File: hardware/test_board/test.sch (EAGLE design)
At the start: 25 parts, among them IC2 MAX707CPA, IC3 74HCT573N, IC5 7805DT, J2 POWER_JACKSLT

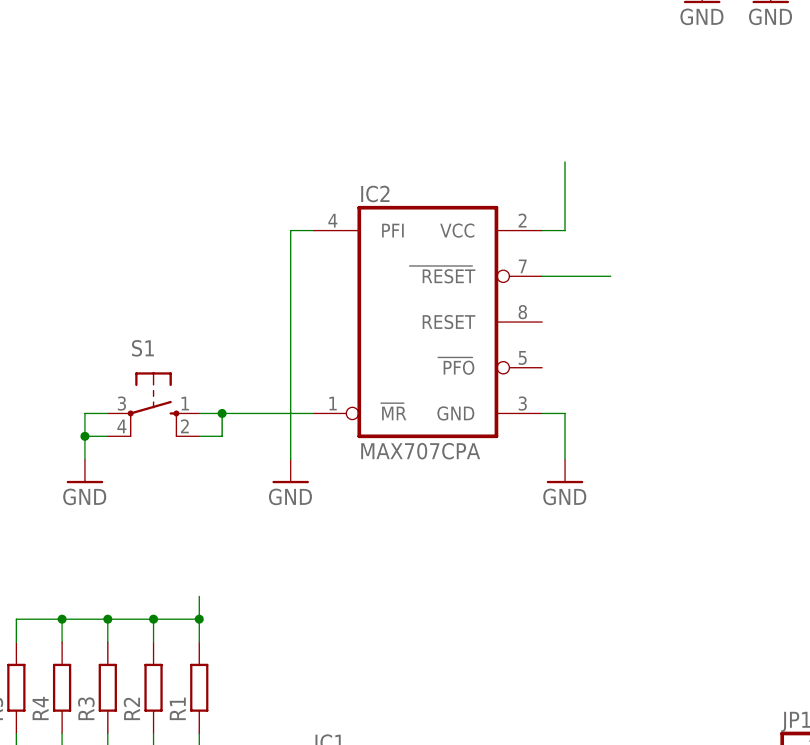
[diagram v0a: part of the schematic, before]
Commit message: RST circuit simplified according to datasheet
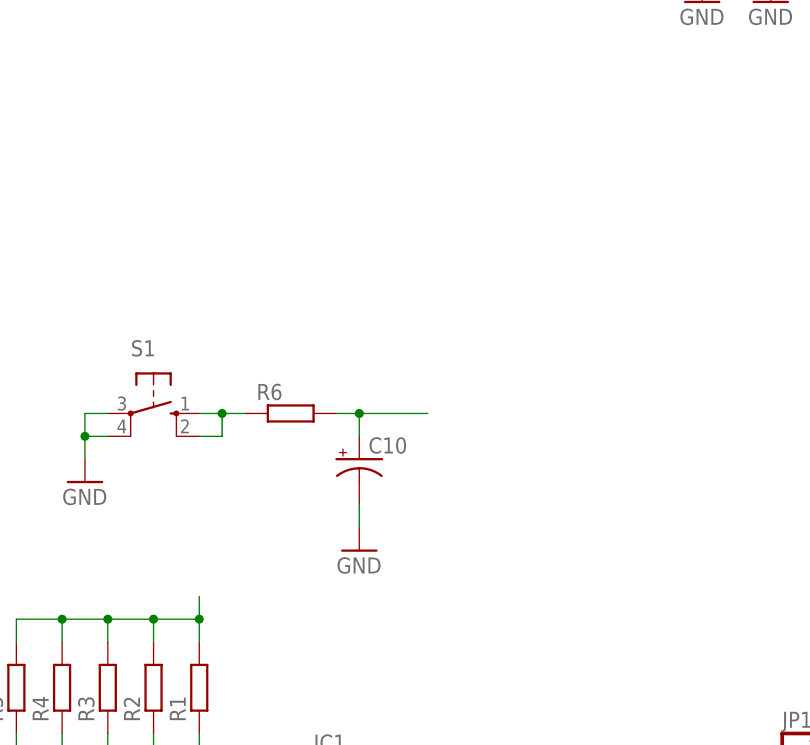
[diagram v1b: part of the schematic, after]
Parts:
- removed IC2: MAX707CPA, maxim:MAX707CPA
- added C10: (no value), rcl:CPOL-USE2,5-6E
- added R6: (no value), rcl:R-EU_R0603
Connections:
- net !RESET: now also C10.+, R6.2; no longer IC2.RESET
- net GND: now also C10.-; no longer IC2.GND, IC2.PFI
- net N$8: now also R6.1; no longer IC2.MR
- net VCC: no longer IC2.VCC
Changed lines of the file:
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@@
 <part name="C3" library="rcl" deviceset="C-EU" device="C0603"/>
 <part name="C4" library="rcl" deviceset="C-EU" device="C0603"/>
-<part name="IC2" library="maxim" deviceset="MAX707CPA" device=""/>
 <part name="GND7" library="supply1" deviceset="GND" device=""/>
-<part name="GND8" library="supply1" deviceset="GND" device=""/>
 <part name="S1" library="switch-omron" deviceset="10-XX" device=""/>
 <part name="GND9" library="supply1" deviceset="GND" device=""/>
@@
 <part name="C9" library="rcl" deviceset="C-EU" device="C0603"/>
 <part name="GND15" library="supply1" deviceset="GND" device=""/>
+<part name="R6" library="rcl" deviceset="R-EU_" device="R0603"/>
+<part name="C10" library="rcl" deviceset="CPOL-US" device="E2,5-6E"/>
 </parts>
 <sheets>
@@
 <instance part="C3" gate="G$1" x="152.4" y="27.94"/>
 <instance part="C4" gate="G$1" x="160.02" y="27.94"/>
-<instance part="IC2" gate="G$1" x="20.32" y="142.24"/>
-<instance part="GND7" gate="1" x="5.08" y="124.46"/>
-<instance part="GND8" gate="1" x="35.56" y="124.46"/>
+<instance part="GND7" gate="1" x="12.7" y="116.84"/>
 <instance part="S1" gate="1" x="-10.16" y="132.08" rot="R270"/>
 <instance part="GND9" gate="1" x="-17.78" y="124.46"/>
@@
 <instance part="C9" gate="G$1" x="167.64" y="27.94"/>
 <instance part="GND15" gate="1" x="55.88" y="63.5"/>
+<instance part="R6" gate="G$1" x="5.08" y="132.08"/>
+<instance part="C10" gate="G$1" x="12.7" y="127"/>
 </instances>
 <busses>
@@
 </segment>
 <segment>
-<pinref part="IC2" gate="G$1" pin="PFI"/>
-<pinref part="GND7" gate="1" pin="GND"/>
-<wire x1="7.62" y1="152.4" x2="5.08" y2="152.4" width="0.1524" layer="91"/>
-<wire x1="5.08" y1="152.4" x2="5.08" y2="127" width="0.1524" layer="91"/>
-</segment>
-<segment>
-<pinref part="IC2" gate="G$1" pin="GND"/>
-<pinref part="GND8" gate="1" pin="GND"/>
-<wire x1="33.02" y1="132.08" x2="35.56" y2="132.08" width="0.1524" layer="91"/>
-<wire x1="35.56" y1="132.08" x2="35.56" y2="127" width="0.1524" layer="91"/>
-</segment>
-<segment>
 <pinref part="S1" gate="1" pin="P"/>
 <pinref part="GND9" gate="1" pin="GND"/>
@@
 <wire x1="63.5" y1="93.98" x2="55.88" y2="93.98" width="0.1524" layer="91"/>
 <wire x1="55.88" y1="93.98" x2="55.88" y2="66.04" width="0.1524" layer="91"/>
+</segment>
+<segment>
+<pinref part="GND7" gate="1" pin="GND"/>
+<pinref part="C10" gate="G$1" pin="-"/>
+<wire x1="12.7" y1="119.38" x2="12.7" y2="121.92" width="0.1524" layer="91"/>
 </segment>
 </net>
@@
 </segment>
 <segment>
-<pinref part="IC2" gate="G$1" pin="VCC"/>
-<wire x1="33.02" y1="152.4" x2="35.56" y2="152.4" width="0.1524" layer="91"/>
-<wire x1="35.56" y1="152.4" x2="35.56" y2="160.02" width="0.1524" layer="91"/>
-</segment>
-<segment>
 <pinref part="IC5" gate="A1" pin="VO"/>
 <wire x1="86.36" y1="193.04" x2="88.9" y2="193.04" width="0.1524" layer="91"/>
@@
 <net name="!RESET" class="0">
 <segment>
-<pinref part="IC2" gate="G$1" pin="RESET"/>
-<wire x1="33.02" y1="147.32" x2="40.64" y2="147.32" width="0.1524" layer="91"/>
-</segment>
-<segment>
 <pinref part="IC1" gate="G$1" pin="RESET"/>
 <wire x1="2.54" y1="83.82" x2="0" y2="83.82" width="0.1524" layer="91"/>
 </segment>
-</net>
-<net name="N$8" class="0">
-<segment>
-<pinref part="IC2" gate="G$1" pin="MR"/>
-<wire x1="7.62" y1="132.08" x2="-2.54" y2="132.08" width="0.1524" layer="91"/>
-<pinref part="S1" gate="1" pin="S"/>
-<pinref part="S1" gate="1" pin="S1"/>
-<wire x1="-2.54" y1="132.08" x2="-5.08" y2="132.08" width="0.1524" layer="91"/>
-<wire x1="-5.08" y1="129.54" x2="-2.54" y2="129.54" width="0.1524" layer="91"/>
-<wire x1="-2.54" y1="129.54" x2="-2.54" y2="132.08" width="0.1524" layer="91"/>
-<junction x="-2.54" y="132.08"/>
+<segment>
+<pinref part="R6" gate="G$1" pin="2"/>
+<pinref part="C10" gate="G$1" pin="+"/>
+<wire x1="10.16" y1="132.08" x2="12.7" y2="132.08" width="0.1524" layer="91"/>
+<wire x1="12.7" y1="132.08" x2="12.7" y2="129.54" width="0.1524" layer="91"/>
+<wire x1="12.7" y1="132.08" x2="20.32" y2="132.08" width="0.1524" layer="91"/>
+<junction x="12.7" y="132.08"/>
 </segment>
 </net>
@@
 </segment>
 </net>
+<net name="N$8" class="0">
+<segment>
+<pinref part="S1" gate="1" pin="S"/>
+<wire x1="-5.08" y1="132.08" x2="-2.54" y2="132.08" width="0.1524" layer="91"/>
+<pinref part="S1" gate="1" pin="S1"/>
+<wire x1="-5.08" y1="129.54" x2="-2.54" y2="129.54" width="0.1524" layer="91"/>
+<wire x1="-2.54" y1="129.54" x2="-2.54" y2="132.08" width="0.1524" layer="91"/>
+<pinref part="R6" gate="G$1" pin="1"/>
+<wire x1="0" y1="132.08" x2="-2.54" y2="132.08" width="0.1524" layer="91"/>
+<junction x="-2.54" y="132.08"/>
+</segment>
+</net>

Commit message: Minor optimizations
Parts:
- removed IC4: (no value), memory:2716
- removed JP1: (no value), pinhead:PINHD-1X10
- added C11: (no value), rcl:C-EUC0603
- added IC2: (no value), memory:2732
- added JP2: (no value), pinhead:PINHD-1X15
- R1, R2, R3, R5: device rcl:R-EU_R0603 -> rcl:R-EU_R1206
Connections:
- removed net N$7: IC1.INT, R5.1
- new net A11: IC1.P23, IC2A.A11
- new net INT: IC1.INT, JP2.14, R5.1
- new net N$17: IC1.P24, JP2.10
- new net N$19: IC1.P25, JP2.11
- new net N$21: IC1.P26, JP2.12
- new net N$22: IC1.P27, JP2.13
- net A0: now also IC2A.A0; no longer IC4A.A0
- net A1: now also IC2A.A1; no longer IC4A.A1
- net A10: now also IC2A.A10; no longer IC4A.A10
- net A2: now also IC2A.A2; no longer IC4A.A2
- net A3: now also IC2A.A3; no longer IC4A.A3
- net A4: now also IC2A.A4; no longer IC4A.A4
- net A5: now also IC2A.A5; no longer IC4A.A5
- net A6: now also IC2A.A6; no longer IC4A.A6
- net A7: now also IC2A.A7; no longer IC4A.A7
- net A8: now also IC2A.A8; no longer IC4A.A8
- net A9: now also IC2A.A9; no longer IC4A.A9
- net D0: now also IC2A.O0; no longer IC4A.O0
- net D1: now also IC2A.O1; no longer IC4A.O1
- net D2: now also IC2A.O2; no longer IC4A.O2
- net D3: now also IC2A.O3; no longer IC4A.O3
- net D4: now also IC2A.O4; no longer IC4A.O4
- net D5: now also IC2A.O5; no longer IC4A.O5
- net D6: now also IC2A.O6; no longer IC4A.O6
- net D7: now also IC2A.O7; no longer IC4A.O7
- net EPROM_OE: now also IC2A.!OE!/VPP; no longer IC4A.!OE
- net GND: now also C11.2, JP2.1; no longer IC4A.!CE, JP1.1
- net N$10: now also JP2.3; no longer JP1.3
- net N$11: now also JP2.4; no longer JP1.4
- net N$12: now also JP2.5; no longer JP1.5
- net N$13: now also JP2.6; no longer JP1.6
- net N$14: now also JP2.7; no longer JP1.7
- net N$15: now also JP2.8; no longer JP1.8
- net N$16: now also JP2.9; no longer JP1.9
- net N$9: now also JP2.2; no longer JP1.2
- net VCC: now also C11.1, JP2.15; no longer IC4A.VPP, JP1.10

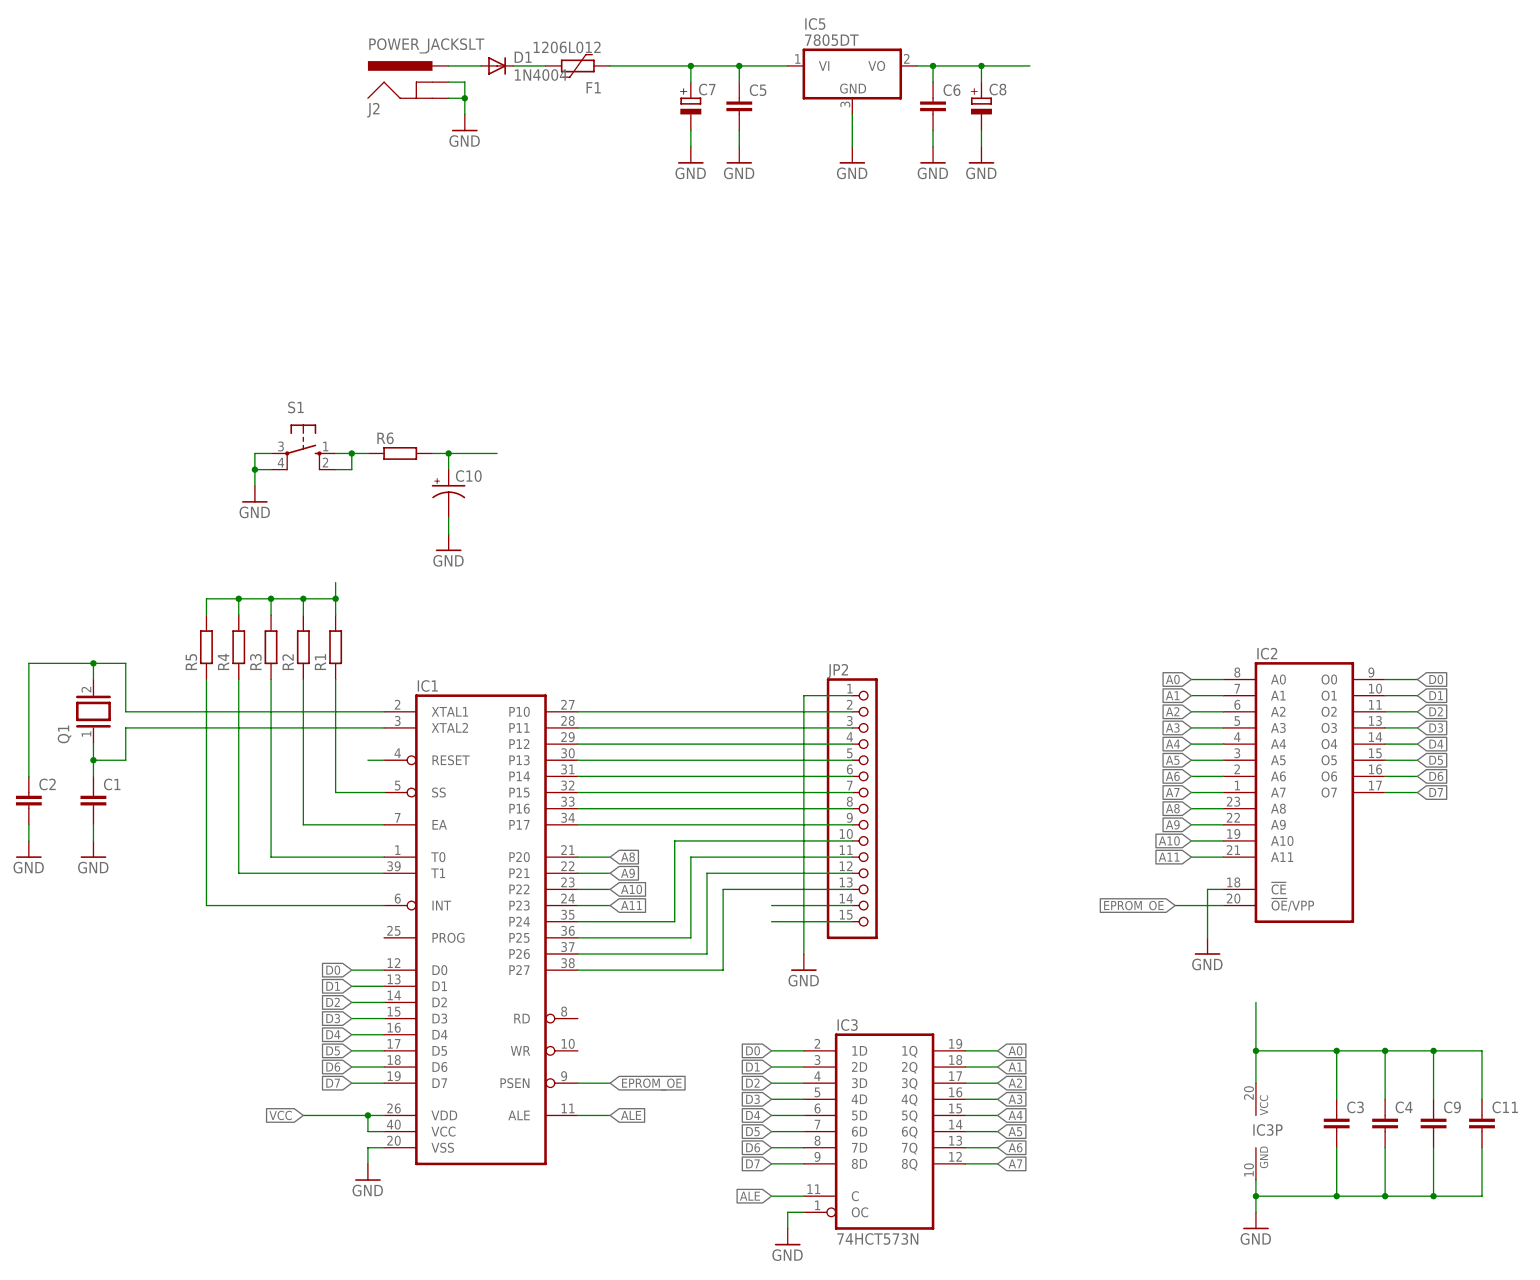
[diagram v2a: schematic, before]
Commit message: Code examples and fix of bug in PCB design
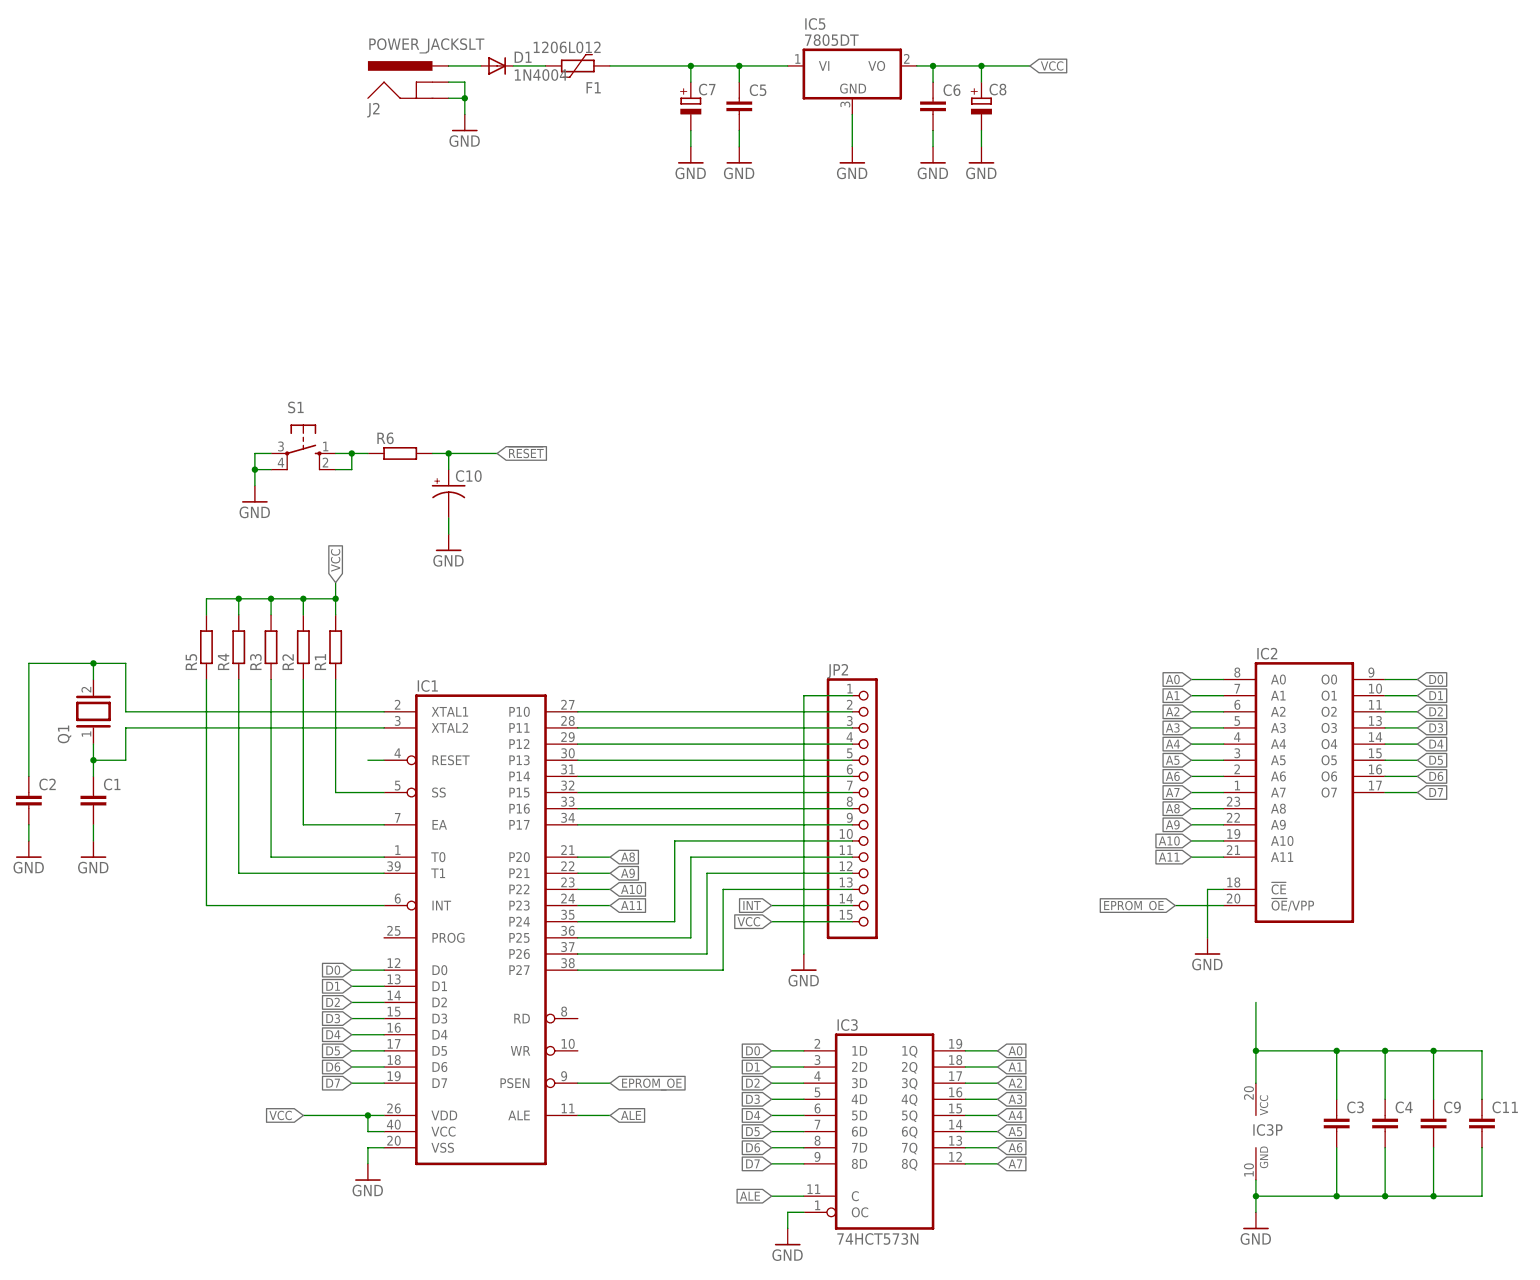
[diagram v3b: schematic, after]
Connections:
- net GND: now also IC2A.!CE
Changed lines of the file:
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@@
 <wire x1="134.62" y1="63.5" x2="132.08" y2="63.5" width="0.1524" layer="91"/>
 <wire x1="132.08" y1="63.5" x2="132.08" y2="55.88" width="0.1524" layer="91"/>
+<pinref part="IC2" gate="A" pin="!CE"/>
 </segment>
 <segment>
@@
 <wire x1="-20.32" y1="106.68" x2="-20.32" y2="109.22" width="0.1524" layer="91"/>
 <junction x="-20.32" y="109.22"/>
+<label x="-5.08" y="111.76" size="1.4224" layer="95" rot="R90" xref="yes"/>
 </segment>
 <segment>
@@
 <wire x1="96.52" y1="190.5" x2="96.52" y2="193.04" width="0.1524" layer="91"/>
 <junction x="96.52" y="193.04"/>
+<label x="104.14" y="193.04" size="1.4224" layer="95" xref="yes"/>
 </segment>
 <segment>
 <pinref part="JP2" gate="A" pin="15"/>
 <wire x1="76.2" y1="58.42" x2="63.5" y2="58.42" width="0.1524" layer="91"/>
+<label x="63.5" y="58.42" size="1.4224" layer="95" rot="R180" xref="yes"/>
 </segment>
 </net>
@@
 <wire x1="12.7" y1="132.08" x2="20.32" y2="132.08" width="0.1524" layer="91"/>
 <junction x="12.7" y="132.08"/>
+<label x="20.32" y="132.08" size="1.4224" layer="95" xref="yes"/>
 </segment>
 </net>
@@
 <pinref part="JP2" gate="A" pin="14"/>
 <wire x1="76.2" y1="60.96" x2="63.5" y2="60.96" width="0.1524" layer="91"/>
-</segment>
-<segment>
+<label x="63.5" y="60.96" size="1.4224" layer="95" rot="R180" xref="yes"/>
+</segment>
+<segment>

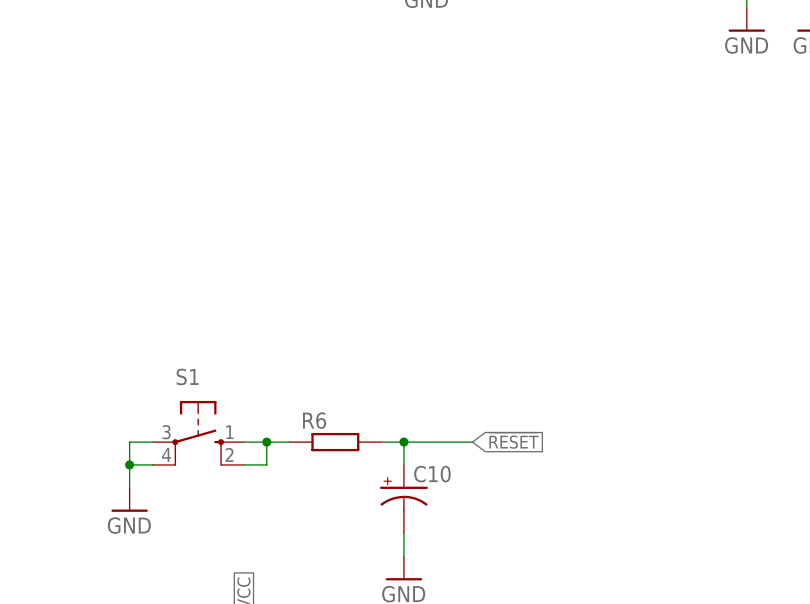
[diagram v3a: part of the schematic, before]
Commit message: Diode aded at RST line
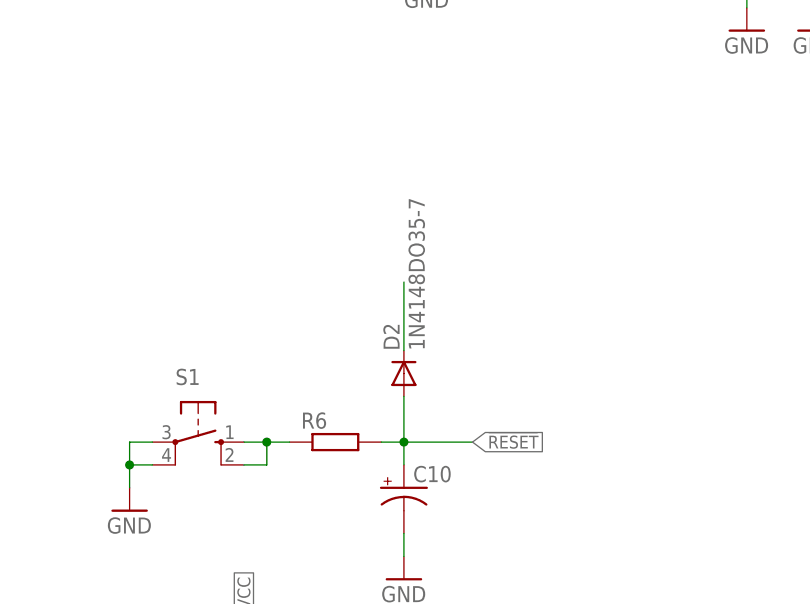
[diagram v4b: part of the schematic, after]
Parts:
- added D2: 1N4148DO35-7, diode:1N4148DO35-7
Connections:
- net !RESET: now also D2.A
- net VCC: now also D2.C
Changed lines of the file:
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@@
 <part name="IC2" library="memory" deviceset="2732" device=""/>
 <part name="C11" library="rcl" deviceset="C-EU" device="C0603"/>
+<part name="D2" library="diode" deviceset="1N4148" device="DO35-7"/>
 </parts>
 <sheets>
@@
 <instance part="IC2" gate="A" x="149.86" y="78.74"/>
 <instance part="C11" gate="G$1" x="175.26" y="27.94"/>
+<instance part="D2" gate="G$1" x="12.7" y="139.7" rot="R90"/>
 </instances>
 <busses>
@@
 <label x="63.5" y="58.42" size="1.4224" layer="95" rot="R180" xref="yes"/>
 </segment>
+<segment>
+<pinref part="D2" gate="G$1" pin="C"/>
+<wire x1="12.7" y1="142.24" x2="12.7" y2="149.86" width="0.1524" layer="91"/>
+</segment>
 </net>
 <net name="N$1" class="0">
@@
 <junction x="12.7" y="132.08"/>
 <label x="20.32" y="132.08" size="1.4224" layer="95" xref="yes"/>
-</segment>
-</net>
+<pinref part="D2" gate="G$1" pin="A"/>
+<wire x1="12.7" y1="132.08" x2="12.7" y2="137.16" width="0.1524" layer="91"/>
+</segment>
+</net>
